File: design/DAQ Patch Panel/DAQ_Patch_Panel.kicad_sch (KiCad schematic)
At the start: 4 parts, among them J1 Power Terminal 1, J2 Data Output Terminal, J3 Power Terminal 2, J4 Weidmuller LM3RZF

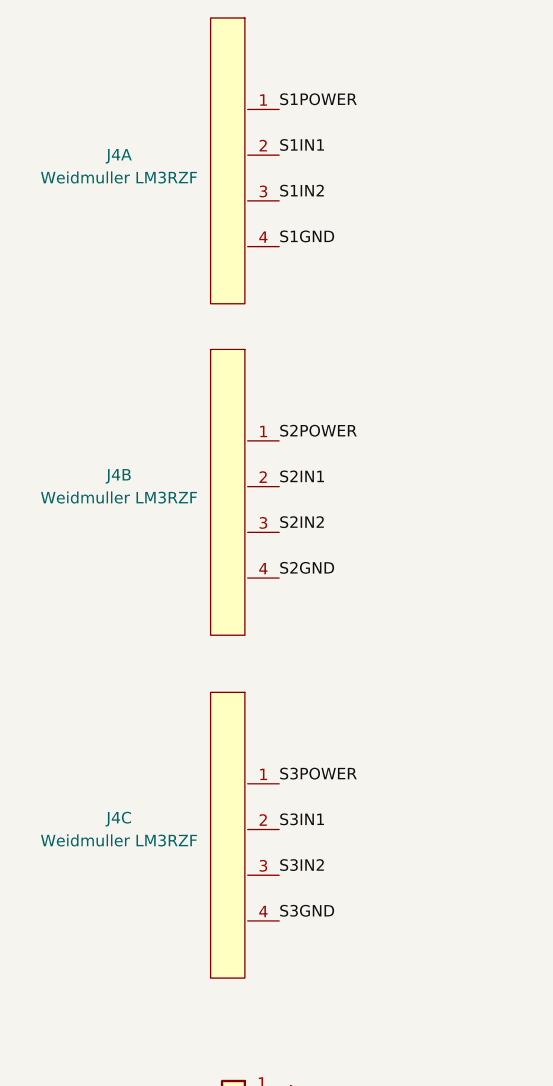
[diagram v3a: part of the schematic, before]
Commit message: Minor Grouping of Components for Routing
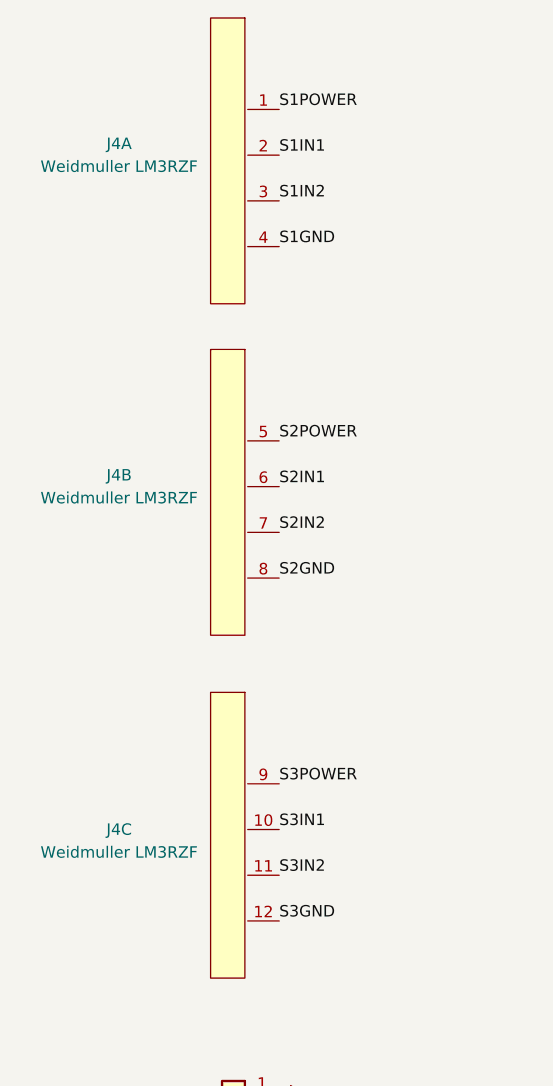
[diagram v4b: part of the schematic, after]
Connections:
- net S2GND: now also J4.8; no longer J4.4
- net S2IN1: now also J4.6; no longer J4.2
- net S2IN2: now also J4.7; no longer J4.3
- net S2POWER: now also J4.5; no longer J4.1
- net S3GND: now also J4.12; no longer J4.4
- net S3IN1: now also J4.10; no longer J4.2
- net S3IN2: now also J4.11; no longer J4.3
- net S3POWER: now also J4.9; no longer J4.1
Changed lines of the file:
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@@
+    )
+  )
+  (symbol (lib_id "DAQLibrary:Weidmuller LM3RZF") (at 83.82 116.84 0) (mirror y) (unit 2)
+    (in_bom yes) (on_board yes) (dnp no)
+    (property "Reference" "J4" (at 71.12 96.52 0)
+      (effects (font (size 1.27 1.27)))
+    )
+    (property "Value" "Weidmuller LM3RZF" (at 71.12 99.06 0)
+      (effects (font (size 1.27 1.27)))
+    )
+    (property "Footprint" "Library:Weidmuller LM3RZF" (at 83.82 116.84 0)
+      (effects (font (size 1.27 1.27)) hide)
+    )
+    (property "Datasheet" "" (at 83.82 116.84 0)
+      (effects (font (size 1.27 1.27)) hide)
+    )
+    (pin "1")
+    (pin "2")
+    (pin "3")
+    (pin "4")
+    (pin "5")
+    (pin "6")
+    (pin "7")
+    (pin "8")
+    (pin "10")
+    (pin "11")
+    (pin "12")
+    (pin "9")
+    (instances
+      (project "DAQ_Patch_Panel"
+        (path "/da75d2ac-4c40-407d-8f74-3497a5ffc88d"
+          (reference "J4") (unit 2)
+        )
+      )
+    )
+  )
+  (symbol (lib_id "DAQLibrary:Weidmuller LM3RZF") (at 83.82 80.01 0) (mirror y) (unit 1)
+    (in_bom yes) (on_board yes) (dnp no)
+    (property "Reference" "J4" (at 71.12 59.69 0)
+      (effects (font (size 1.27 1.27)))
+    )
+    (property "Value" "Weidmuller LM3RZF" (at 71.12 62.23 0)
+      (effects (font (size 1.27 1.27)))
+    )
+    (property "Footprint" "Library:Weidmuller LM3RZF" (at 83.82 80.01 0)
+      (effects (font (size 1.27 1.27)) hide)
+    )
+    (property "Datasheet" "" (at 83.82 80.01 0)
+      (effects (font (size 1.27 1.27)) hide)
+    )
+    (pin "1")
+    (pin "2")
+    (pin "3")
+    (pin "4")
+    (pin "5")
+    (pin "6")
+    (pin "7")
+    (pin "8")
+    (pin "10")
+    (pin "11")
+    (pin "12")
+    (pin "9")
+    (instances
+      (project "DAQ_Patch_Panel"
+        (path "/da75d2ac-4c40-407d-8f74-3497a5ffc88d"
+          (reference "J4") (unit 1)
+        )
+      )
+    )
+  )
+  (symbol (lib_id "DAQLibrary:Weidmuller LM3RZF") (at 83.82 154.94 0) (mirror y) (unit 3)
+    (in_bom yes) (on_board yes) (dnp no)
+    (property "Reference" "J4" (at 71.12 135.89 0)
+      (effects (font (size 1.27 1.27)))
+    )
+    (property "Value" "Weidmuller LM3RZF" (at 71.12 138.43 0)
+      (effects (font (size 1.27 1.27)))
+    )
+    (property "Footprint" "Library:Weidmuller LM3RZF" (at 83.82 154.94 0)
+      (effects (font (size 1.27 1.27)) hide)
+    )
+    (property "Datasheet" "" (at 83.82 154.94 0)
+      (effects (font (size 1.27 1.27)) hide)
+    )
+    (pin "1")
+    (pin "2")
+    (pin "3")
+    (pin "4")
+    (pin "5")
+    (pin "6")
+    (pin "7")
+    (pin "8")
+    (pin "10")
+    (pin "11")
+    (pin "12")
+    (pin "9")
+    (instances
+      (project "DAQ_Patch_Panel"
+        (path "/da75d2ac-4c40-407d-8f74-3497a5ffc88d"
+          (reference "J4") (unit 3)
+        )
+      )
     )
   )
@@
     )
   )
-  (symbol (lib_id "DAQLibrary:Weidmuller LM3RZF") (at 83.82 116.84 0) (mirror y) (unit 2)
-    (in_bom yes) (on_board yes) (dnp no)
-    (property "Reference" "J4" (at 71.12 96.52 0)
-      (effects (font (size 1.27 1.27)))
-    )
-    (property "Value" "Weidmuller LM3RZF" (at 71.12 99.06 0)
-      (effects (font (size 1.27 1.27)))
-    )
-    (property "Footprint" "Library:Weidmuller LM3RZF" (at 83.82 116.84 0)
-      (effects (font (size 1.27 1.27)) hide)
-    )
-    (property "Datasheet" "" (at 83.82 116.84 0)
-      (effects (font (size 1.27 1.27)) hide)
-    )
-    (pin "1")
-    (pin "2")
-    (pin "3")
-    (pin "4")
-    (instances
-      (project "DAQ_Patch_Panel"
-        (path "/da75d2ac-4c40-407d-8f74-3497a5ffc88d"
-          (reference "J4") (unit 2)
-        )
-      )
-    )
-  )
   (symbol (lib_id "Connector:Screw_Terminal_01x05") (at 83.82 170.18 0) (mirror y) (unit 1)
     (in_bom yes) (on_board yes) (dnp no)
@@
     )
   )
-  (symbol (lib_id "DAQLibrary:Weidmuller LM3RZF") (at 83.82 80.01 0) (mirror y) (unit 1)
-    (in_bom yes) (on_board yes) (dnp no)
-    (property "Reference" "J4" (at 71.12 60.96 0)
-      (effects (font (size 1.27 1.27)))
-    )
-    (property "Value" "Weidmuller LM3RZF" (at 71.12 63.5 0)
-      (effects (font (size 1.27 1.27)))
-    )
-    (property "Footprint" "Library:Weidmuller LM3RZF" (at 83.82 80.01 0)
-      (effects (font (size 1.27 1.27)) hide)
-    )
-    (property "Datasheet" "" (at 83.82 80.01 0)
-      (effects (font (size 1.27 1.27)) hide)
-    )
-    (pin "1")
-    (pin "2")
-    (pin "3")
-    (pin "4")
-    (instances
-      (project "DAQ_Patch_Panel"
-        (path "/da75d2ac-4c40-407d-8f74-3497a5ffc88d"
-          (reference "J4") (unit 1)
-        )
-      )
-    )
-  )
   (symbol (lib_id "power:+12V") (at 88.9 167.64 270) (unit 1)
     (in_bom yes) (on_board yes) (dnp no)
@@
         )
       )
-    )
-  )
-  (symbol (lib_id "DAQLibrary:Weidmuller LM3RZF") (at 83.82 154.94 0) (mirror y) (unit 3)
-    (in_bom yes) (on_board yes) (dnp no)
-    (property "Reference" "J4" (at 71.12 134.62 0)
-      (effects (font (size 1.27 1.27)))
-    )
-    (property "Value" "Weidmuller LM3RZF" (at 71.12 137.16 0)
-      (effects (font (size 1.27 1.27)))
-    )
-    (property "Footprint" "Library:Weidmuller LM3RZF" (at 83.82 154.94 0)
-      (effects (font (size 1.27 1.27)) hide)
-    )
-    (property "Datasheet" "" (at 83.82 154.94 0)
-      (effects (font (size 1.27 1.27)) hide)
-    )
-    (pin "1")
-    (pin "2")
-    (pin "3")
-    (pin "4")
-    (instances
-      (project "DAQ_Patch_Panel"
-        (path "/da75d2ac-4c40-407d-8f74-3497a5ffc88d"
-          (reference "J4") (unit 3)
-        )
-      )

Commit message: More Layout Edits
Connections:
- net S1GND: now also J4.2; no longer J4.4
- net S1IN1: now also J4.3; no longer J4.2
- net S1IN2: now also J4.4; no longer J4.3
- net S2GND: now also J4.6; no longer J4.8
- net S2IN1: now also J4.7; no longer J4.6
- net S2IN2: now also J4.8; no longer J4.7
- net S3GND: now also J4.10; no longer J4.12
- net S3IN1: now also J4.11; no longer J4.10
- net S3IN2: now also J4.12; no longer J4.11
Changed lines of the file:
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@@
     (effects (font (size 1.27 1.27)) (justify right bottom))
   )
-  (label "S2IN1" (at 88.9 97.79 0) (fields_autoplaced)
+  (label "S2IN1" (at 88.9 102.87 0) (fields_autoplaced)
     (effects (font (size 1.27 1.27)) (justify left bottom))
   )
-  (label "S1IN2" (at 88.9 66.04 0) (fields_autoplaced)
+  (label "S1IN2" (at 88.9 71.12 0) (fields_autoplaced)
     (effects (font (size 1.27 1.27)) (justify left bottom))
   )
@@
     (effects (font (size 1.27 1.27)) (justify right bottom))
   )
-  (label "S3IN2" (at 88.9 140.97 0) (fields_autoplaced)
+  (label "S3IN2" (at 88.9 146.05 0) (fields_autoplaced)
     (effects (font (size 1.27 1.27)) (justify left bottom))
   )
@@
     (effects (font (size 1.27 1.27)) (justify left bottom))
   )
-  (label "S2IN2" (at 88.9 102.87 0) (fields_autoplaced)
+  (label "S2IN2" (at 88.9 107.95 0) (fields_autoplaced)
     (effects (font (size 1.27 1.27)) (justify left bottom))
   )
@@
     (effects (font (size 1.27 1.27)) (justify right bottom))
   )
-  (label "S2GND" (at 88.9 107.95 0) (fields_autoplaced)
+  (label "S2GND" (at 88.9 97.79 0) (fields_autoplaced)
     (effects (font (size 1.27 1.27)) (justify left bottom))
   )
@@
     (effects (font (size 1.27 1.27)) (justify right bottom))
   )
-  (label "S3IN1" (at 88.9 135.89 0) (fields_autoplaced)
+  (label "S3IN1" (at 88.9 140.97 0) (fields_autoplaced)
     (effects (font (size 1.27 1.27)) (justify left bottom))
   )
@@
     (effects (font (size 1.27 1.27)) (justify right bottom))
   )
-  (label "S1IN1" (at 88.9 60.96 0) (fields_autoplaced)
+  (label "S1IN1" (at 88.9 66.04 0) (fields_autoplaced)
     (effects (font (size 1.27 1.27)) (justify left bottom))
   )
@@
     (effects (font (size 1.27 1.27)) (justify right bottom))
   )
-  (label "S1GND" (at 88.9 71.12 0) (fields_autoplaced)
+  (label "S1GND" (at 88.9 60.96 0) (fields_autoplaced)
     (effects (font (size 1.27 1.27)) (justify left bottom))
   )
@@
     (effects (font (size 1.27 1.27)) (justify right bottom))
   )
-  (label "S3GND" (at 88.9 146.05 0) (fields_autoplaced)
+  (label "S3GND" (at 88.9 135.89 0) (fields_autoplaced)
     (effects (font (size 1.27 1.27)) (justify left bottom))
   )

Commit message: More Changes
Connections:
- net +12V: now also J1.4 (Pin_4); no longer J1.2 (Pin_2)
- net +20V: now also J1.5 (Pin_5); no longer J1.1 (Pin_1)
- net +5V: now also J1.2 (Pin_2); no longer J1.4 (Pin_4)
- net GND: now also J1.1 (Pin_1); no longer J1.5 (Pin_5)
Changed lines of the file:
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@@
     (company "Waterloo Rocketry ")
   )
-  (wire (pts (xy 91.44 176.53) (xy 91.44 175.26))
+  (wire (pts (xy 101.6 168.91) (xy 101.6 165.1))
     (stroke (width 0) (type default))
   )
@@
     (stroke (width 0) (type default))
   )
-  (wire (pts (xy 91.44 175.26) (xy 88.9 175.26))
+  (wire (pts (xy 101.6 165.1) (xy 88.9 165.1))
     (stroke (width 0) (type default))
   )
@@
     )
   )
-  (symbol (lib_id "power:GND") (at 91.44 176.53 0) (mirror y) (unit 1)
-    (in_bom yes) (on_board yes) (dnp no)
-    (property "Reference" "#PWR014" (at 91.44 182.88 0)
-      (effects (font (size 1.27 1.27)) hide)
-    )
-    (property "Value" "GND" (at 91.44 181.61 0)
-      (effects (font (size 1.27 1.27)))
-    )
-    (property "Footprint" "" (at 91.44 176.53 0)
-      (effects (font (size 1.27 1.27)) hide)
-    )
-    (property "Datasheet" "" (at 91.44 176.53 0)
+  (symbol (lib_id "power:GND") (at 101.6 168.91 0) (unit 1)
+    (in_bom yes) (on_board yes) (dnp no)
+    (property "Reference" "#PWR014" (at 101.6 175.26 0)
+      (effects (font (size 1.27 1.27)) hide)
+    )
+    (property "Value" "GND" (at 101.6 173.99 0)
+      (effects (font (size 1.27 1.27)))
+    )
+    (property "Footprint" "" (at 101.6 168.91 0)
+      (effects (font (size 1.27 1.27)) hide)
+    )
+    (property "Datasheet" "" (at 101.6 168.91 0)
       (effects (font (size 1.27 1.27)) hide)
     )
@@
     )
   )
-  (symbol (lib_name "+10V_1") (lib_id "power:+10V") (at 88.9 165.1 270) (unit 1)
-    (in_bom yes) (on_board yes) (dnp no)
-    (property "Reference" "#PWR013" (at 85.09 165.1 0)
-      (effects (font (size 1.27 1.27)) hide)
-    )
-    (property "Value" "+20V" (at 92.71 165.1 90)
-      (effects (font (size 1.27 1.27)) (justify left))
-    )
-    (property "Footprint" "" (at 88.9 165.1 0)
-      (effects (font (size 1.27 1.27)) hide)
-    )
-    (property "Datasheet" "" (at 88.9 165.1 0)
+  (symbol (lib_name "+10V_1") (lib_id "power:+10V") (at 88.9 175.26 270) (mirror x) (unit 1)
+    (in_bom yes) (on_board yes) (dnp no)
+    (property "Reference" "#PWR013" (at 85.09 175.26 0)
+      (effects (font (size 1.27 1.27)) hide)
+    )
+    (property "Value" "+20V" (at 92.71 175.26 90)
+      (effects (font (size 1.27 1.27)) (justify left))
+    )
+    (property "Footprint" "" (at 88.9 175.26 0)
+      (effects (font (size 1.27 1.27)) hide)
+    )
+    (property "Datasheet" "" (at 88.9 175.26 0)
       (effects (font (size 1.27 1.27)) hide)
     )
@@
     )
   )
-  (symbol (lib_id "power:+10V") (at 88.9 170.18 270) (unit 1)
+  (symbol (lib_id "power:+10V") (at 88.9 170.18 270) (mirror x) (unit 1)
     (in_bom yes) (on_board yes) (dnp no)
     (property "Reference" "#PWR011" (at 85.09 170.18 0)
@@
     )
   )
-  (symbol (lib_id "power:+5V") (at 88.9 172.72 270) (unit 1)
-    (in_bom yes) (on_board yes) (dnp no)
-    (property "Reference" "#PWR012" (at 85.09 172.72 0)
-      (effects (font (size 1.27 1.27)) hide)
-    )
-    (property "Value" "+5V" (at 92.71 172.72 90)
-      (effects (font (size 1.27 1.27)) (justify left))
-    )
-    (property "Footprint" "" (at 88.9 172.72 0)
-      (effects (font (size 1.27 1.27)) hide)
-    )
-    (property "Datasheet" "" (at 88.9 172.72 0)
+  (symbol (lib_id "power:+5V") (at 88.9 167.64 270) (mirror x) (unit 1)
+    (in_bom yes) (on_board yes) (dnp no)
+    (property "Reference" "#PWR012" (at 85.09 167.64 0)
+      (effects (font (size 1.27 1.27)) hide)
+    )
+    (property "Value" "+5V" (at 92.71 167.64 90)
+      (effects (font (size 1.27 1.27)) (justify left))
+    )
+    (property "Footprint" "" (at 88.9 167.64 0)
+      (effects (font (size 1.27 1.27)) hide)
+    )
+    (property "Datasheet" "" (at 88.9 167.64 0)
       (effects (font (size 1.27 1.27)) hide)
     )
@@
     )
   )
-  (symbol (lib_id "power:+12V") (at 88.9 167.64 270) (unit 1)
-    (in_bom yes) (on_board yes) (dnp no)
-    (property "Reference" "#PWR010" (at 85.09 167.64 0)
-      (effects (font (size 1.27 1.27)) hide)
-    )
-    (property "Value" "+12V" (at 92.71 167.64 90)
-      (effects (font (size 1.27 1.27)) (justify left))
-    )
-    (property "Footprint" "" (at 88.9 167.64 0)
-      (effects (font (size 1.27 1.27)) hide)
-    )
-    (property "Datasheet" "" (at 88.9 167.64 0)
-      (effects (font (size 1.27 1.27)) hide)
-    )
+  (symbol (lib_id "power:+12V") (at 88.9 172.72 270) (mirror x) (unit 1)
+    (in_bom yes) (on_board yes) (dnp no)
+    (property "Reference" "#PWR010" (at 85.09 172.72 0)
+      (effects (font (size 1.27 1.27)) hide)
+    )
+    (property "Value" "+12V" (at 92.71 172.72 90)
+      (effects (font (size 1.27 1.27)) (justify left))
+    )
+    (property "Footprint" "" (at 88.9 172.72 0)
+      (effects (font (size 1.27 1.27)) hide)
+    )
+    (property "Datasheet" "" (at 88.9 172.72 0)
+      (effects (font (size 1.27 1.27)) hide)
+    )

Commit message: First draft PCB
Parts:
- removed J4: Weidmuller LM3RZF, Library:Weidmuller LM3RZF, symbol DAQLibrary:Weidmuller LM3RZF
- added J4: Sensor 1, Library:CONN_1751189, symbol DAQLibrary:1751189
- added J5: Sensor 2, Library:CONN_1751189, symbol DAQLibrary:1751189
- added J6: Sensor 3, Library:CONN_1751189, symbol DAQLibrary:1751189
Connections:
- net S1DATA2: now also J2.6 (Pin_6); no longer J2.2 (Pin_2)
- net S1GND: now also J4.6
- net S1IN1: now also J4.4
- net S1IN2: now also J4.2
- net S1POWER: now also J4.8
- net S2DATA1: now also J2.2 (Pin_2); no longer J2.3 (Pin_3)
- net S2DATA2: now also J2.5 (Pin_5); no longer J2.4 (Pin_4)
- net S2GND: now also J5.6
- net S2IN1: now also J5.4
- net S2IN2: now also J5.2
- net S2POWER: now also J5.8
- net S3DATA1: now also J2.3 (Pin_3); no longer J2.5 (Pin_5)
- net S3DATA2: now also J2.4 (Pin_4); no longer J2.6 (Pin_6)
- net S3GND: now also J6.6
- net S3IN1: now also J6.4
- net S3IN2: now also J6.2
- net S3POWER: now also J6.8
- net +20V renamed +24V
- no-connect marks 0 -> 12

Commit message: Layout for prod, v1
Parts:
- added H1, H2, H3, H4: MountingHole, MountingHole:MountingHole_3.2mm_M3, symbol Mechanical:MountingHole
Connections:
- net S1DATA1: now also J2.6 (Pin_6); no longer J2.1 (Pin_1)
- net S1DATA2: now also J2.1 (Pin_1); no longer J2.6 (Pin_6)
- net S2DATA1: now also J2.5 (Pin_5); no longer J2.2 (Pin_2)
- net S2DATA2: now also J2.2 (Pin_2); no longer J2.5 (Pin_5)
- net S3DATA1: now also J2.4 (Pin_4); no longer J2.3 (Pin_3)
- net S3DATA2: now also J2.3 (Pin_3); no longer J2.4 (Pin_4)
